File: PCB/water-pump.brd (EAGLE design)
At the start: 53 x 79.1 mm, 26 parts, among them U1 LDL1117S12R, U3 ATSAMD11C14A-SSUT

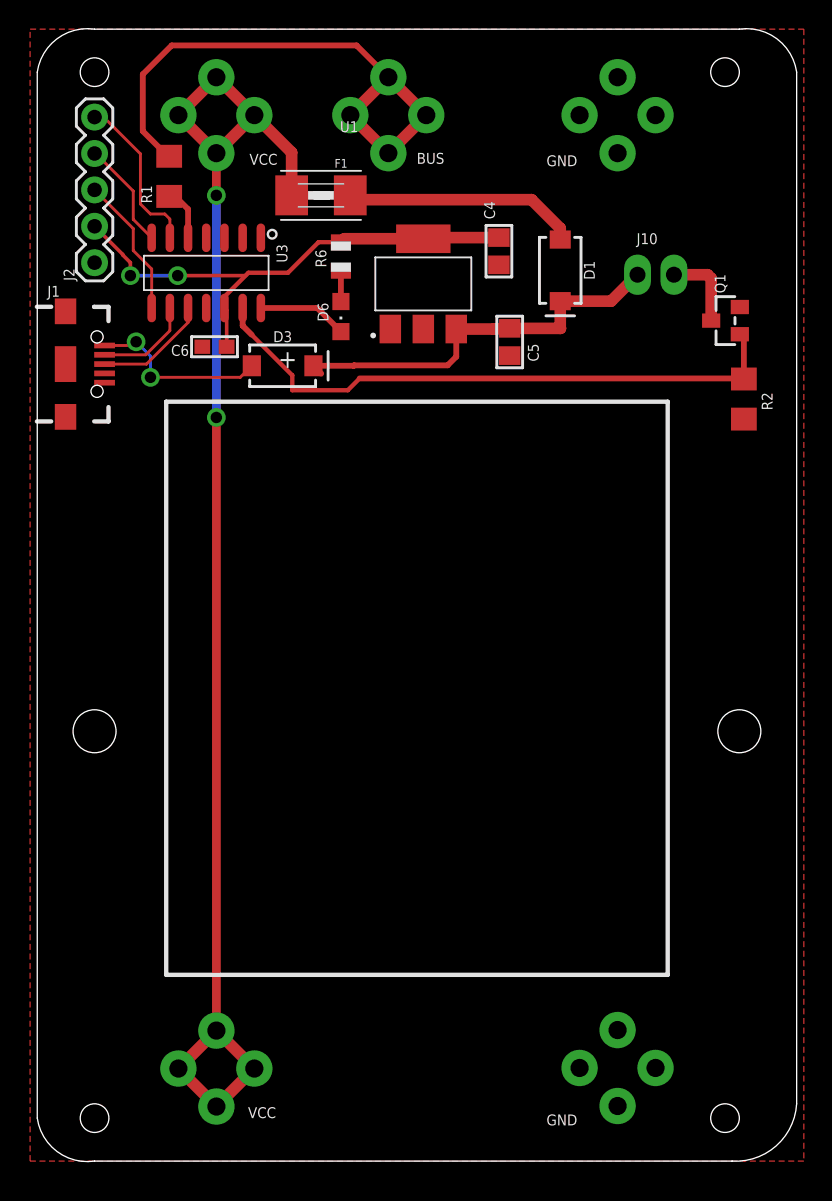
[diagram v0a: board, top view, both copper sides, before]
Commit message: added button to pcbs and did some fixing
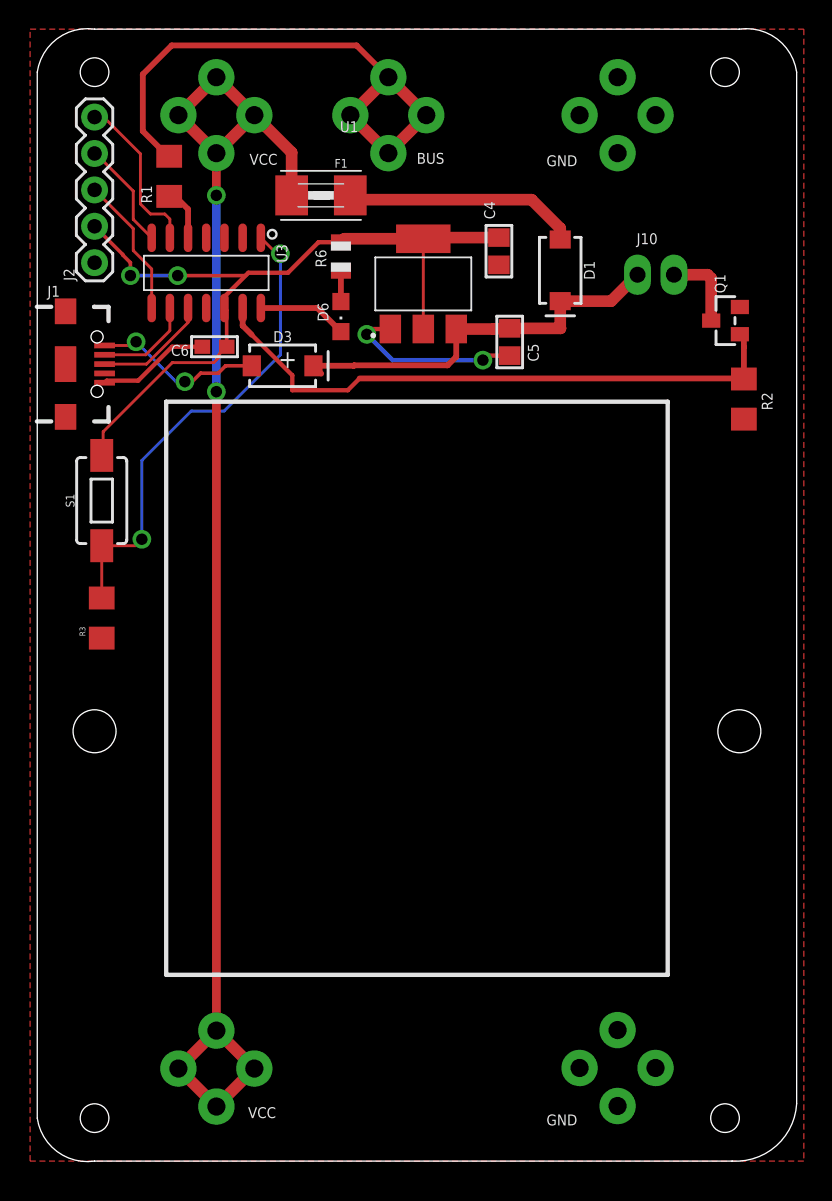
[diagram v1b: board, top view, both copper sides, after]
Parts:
- added R3: 2k, SparkFun-Resistors:1206
- added S1: MOMENTARY-SWITCH-SPST-SMD-6.0X3.5MM, SparkFun-Switches:TACTILE_SWITCH_SMD_6.0X3.5MM
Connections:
- new net N$4: R3.2, S1.1, U3.1
- net 3.3V: now also S1.2
- net GND: now also R3.1
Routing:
- net N$4: track 0.00 -> 33.7 mm, vias 0 -> 2
- net GND: track 0.00 -> 22.5 mm, vias 0 -> 2
- net 3.3V: track 37.2 -> 56.4 mm
- net N$1: track 12.6 -> 12.0 mm
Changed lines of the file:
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@@
 <?xml version="1.0" encoding="utf-8"?>
 <!DOCTYPE eagle SYSTEM "eagle.dtd">
-<eagle version="9.3.0">
+<eagle version="9.2.2">
 <drawing>
 <settings>
@@
 <attribute name="PACKAGE" value="SOIC-14 Microchip" x="11.795" y="61.989" size="1.778" layer="27" rot="R270" display="off"/>
 <attribute name="PRICE" value="1.18 USD" x="11.795" y="61.989" size="1.778" layer="27" rot="R270" display="off"/>
-<attribute name="VALUE" x="5.99306875" y="65.09003125" size="0.762" layer="27" font="vector" ratio="15" rot="R270"/>
 </element>
 <element name="D6" library="Adafruit" package="CHIPLED_0805" value="" x="21.193" y="58.941" smashed="yes" rot="R180">
@@
 <attribute name="NAME" x="21.6575" y="69.94" size="0.6096" layer="25" rot="R180"/>
 <attribute name="VALUE" x="21.6575" y="65.495" size="0.6096" layer="27" rot="R180"/>
+</element>
+<element name="R3" library="SparkFun-Resistors" package="1206" value="2k" x="4.5" y="37.9" smashed="yes" rot="R90">
+<attribute name="NAME" x="3.357" y="36.63" size="0.4064" layer="25" rot="R90"/>
+<attribute name="VALUE" x="6.024" y="36.503" size="0.4064" layer="27" rot="R90"/>
+</element>
+<element name="S1" library="SparkFun-Switches" package="TACTILE_SWITCH_SMD_6.0X3.5MM" value="MOMENTARY-SWITCH-SPST-SMD-6.0X3.5MM" x="4.5" y="46.1" smashed="yes" rot="R90">
+<attribute name="NAME" x="2.595" y="46.1" size="0.6096" layer="25" font="vector" ratio="20" rot="R90" align="bottom-center"/>
+<attribute name="PROD_ID" value="SWCH-00815" x="4.5" y="46.1" size="1.778" layer="27" rot="R90" display="off"/>
+<attribute name="SF_SKU" value="COM-08229" x="4.5" y="46.1" size="1.778" layer="27" rot="R90" display="off"/>
 </element>
 </elements>
@@
 <contactref element="Q1" pad="2"/>
 <contactref element="J1" pad="GND"/>
-<wire x1="40.502" y1="75.646" x2="43.15" y2="73" width="0" layer="19" extent="1-1"/>
-<wire x1="37.85" y1="73" x2="40.502" y2="75.646" width="0" layer="19" extent="1-1"/>
-<wire x1="40.502" y1="70.346" x2="43.15" y2="73" width="0" layer="19" extent="1-1"/>
-<wire x1="32.221" y1="62.553" x2="40.502" y2="70.346" width="0" layer="19" extent="1-1"/>
-<wire x1="32.973" y1="56.217" x2="32.221" y2="62.553" width="0" layer="19" extent="1-1"/>
-<wire x1="24.643" y1="58.071" x2="32.973" y2="56.217" width="0" layer="19" extent="1-1"/>
-<wire x1="11.521" y1="56.836" x2="24.643" y2="58.071" width="0" layer="19" extent="1-1"/>
-<wire x1="11.795" y1="59.539" x2="11.521" y2="56.836" width="0" layer="19" extent="1-1"/>
-<wire x1="4" y1="62.703" x2="11.795" y2="59.539" width="0" layer="19" extent="1-1"/>
-<wire x1="49.034" y1="59.609" x2="40.502" y2="70.346" width="0" layer="19" extent="1-1"/>
-<wire x1="49.317" y1="51.784" x2="49.034" y2="59.609" width="0" layer="19" extent="1-1"/>
-<wire x1="40.502" y1="9.146" x2="49.317" y2="51.784" width="0" layer="19" extent="1-1"/>
-<wire x1="43.15" y1="6.5" x2="40.502" y2="9.146" width="0" layer="19" extent="1-1"/>
-<wire x1="37.85" y1="6.5" x2="40.502" y2="9.146" width="0" layer="19" extent="1-1"/>
-<wire x1="40.502" y1="3.846" x2="43.15" y2="6.5" width="0" layer="19" extent="1-1"/>
-<wire x1="1.974" y1="59.309" x2="37.85" y2="6.5" width="0" layer="19" extent="1-1"/>
-<wire x1="1.974" y1="55.624" x2="1.974" y2="59.309" width="0" layer="19" extent="1-1"/>
-<wire x1="4.699" y1="54.324" x2="1.974" y2="55.624" width="0" layer="19" extent="1-1"/>
-<wire x1="1.974" y1="51.939" x2="4.699" y2="54.324" width="0" layer="19" extent="1-1"/>
+<contactref element="R3" pad="1"/>
+<wire x1="9.53020625" y1="56.836" x2="11.521" y2="56.836" width="0.2032" layer="1"/>
+<wire x1="4.699" y1="54.324" x2="4.8442" y2="54.4692" width="0.3048" layer="1"/>
+<wire x1="9.4107375" y1="56.836" x2="11.521" y2="56.836" width="0.3048" layer="1"/>
+<wire x1="4.8442" y1="54.4692" x2="7.0439375" y2="54.4692" width="0.3048" layer="1"/>
+<wire x1="7.0439375" y1="54.4692" x2="9.4107375" y2="56.836" width="0.3048" layer="1"/>
+<wire x1="32.973" y1="56.217" x2="31.417" y2="56.217" width="0.3048" layer="1"/>
+<wire x1="31.417" y1="56.217" x2="31.1" y2="55.9" width="0.3048" layer="1"/>
+<via x="31.1" y="55.9" extent="1-16" drill="0.8"/>
+<wire x1="31.1" y1="55.9" x2="24.8" y2="55.9" width="0.3048" layer="16"/>
+<wire x1="24.8" y1="55.9" x2="23" y2="57.7" width="0.3048" layer="16"/>
+<via x="23" y="57.7" extent="1-16" drill="0.8"/>
+<wire x1="23" y1="57.7" x2="23.371" y2="58.071" width="0.3048" layer="1"/>
+<wire x1="23.371" y1="58.071" x2="24.643" y2="58.071" width="0.3048" layer="1"/>
 </signal>
 <signal name="VCC-RAW" class="1">
@@
 <wire x1="15.15" y1="73" x2="17.754" y2="70.396" width="0.8128" layer="1"/>
 <wire x1="17.754" y1="70.396" x2="17.754" y2="67.4" width="0.8128" layer="1"/>
-<wire x1="12.5026" y1="51.8974" x2="12.5" y2="51.9" width="0.6096" layer="1"/>
-<via x="12.5" y="51.9" extent="1-16" drill="0.8"/>
-<wire x1="12.5" y1="51.9" x2="12.5" y2="67.4" width="0.6096" layer="16"/>
+<wire x1="12.5026" y1="53.6974" x2="12.5" y2="53.7" width="0.6096" layer="1"/>
+<via x="12.5" y="53.7" extent="1-16" drill="0.8"/>
+<wire x1="12.5" y1="53.7" x2="12.5" y2="67.4" width="0.6096" layer="16"/>
 <via x="12.5" y="67.4" extent="1-16" drill="0.8"/>
 <wire x1="12.5" y1="67.4" x2="12.5" y2="70.342" width="0.6096" layer="1"/>
 <wire x1="12.5" y1="70.342" x2="12.498" y2="70.344" width="0.6096" layer="1"/>
-<wire x1="12.5026" y1="9.1074" x2="12.5026" y2="51.8974" width="0.6096" layer="1"/>
+<wire x1="12.5026" y1="9.1074" x2="12.5026" y2="53.6974" width="0.6096" layer="1"/>
 </signal>
 <signal name="BUS">
@@
 <signal name="PUMP_CTRL">
 <contactref element="R2" pad="1"/>
-<wire x1="49.317" y1="57.426" x2="49.317" y2="54.623" width="0.4064" layer="1"/>
 <contactref element="U3" pad="13"/>
+<wire x1="49.317" y1="56.8" x2="49.317" y2="54.623" width="0.4064" layer="1"/>
 <wire x1="49.317" y1="54.623" x2="49.317" y2="54.584" width="0.4064" layer="1"/>
 <wire x1="14.335" y1="59.539" x2="14.335" y2="58.306" width="0.4064" layer="1"/>
@@
 <wire x1="17.8" y1="53.8" x2="17.8" y2="54.841" width="0.3048" layer="1"/>
 <wire x1="17.8" y1="54.841" x2="14.97" y2="57.671" width="0.3048" layer="1"/>
-<wire x1="49.317" y1="57.426" x2="49.034" y2="57.709" width="0" layer="19" extent="1-1"/>
+<wire x1="49.317" y1="56.8" x2="49.317" y2="57.426" width="0.4064" layer="1"/>
+<wire x1="49.317" y1="57.426" x2="49.034" y2="57.709" width="0.4064" layer="1"/>
 </signal>
 <signal name="PUMP">
@@
 <wire x1="6.642" y1="56.924" x2="6.9" y2="57.182" width="0.2032" layer="1"/>
 <via x="6.9" y="57.182" extent="1-16" drill="0.8"/>
-<wire x1="6.9" y1="57.182" x2="7.9" y2="56.182" width="0.2032" layer="16"/>
-<wire x1="7.9" y1="56.182" x2="7.9" y2="54.7" width="0.2032" layer="16"/>
-<via x="7.9" y="54.7" extent="1-16" drill="0.8"/>
-<wire x1="7.9" y1="54.7" x2="14.168" y2="54.7" width="0.2032" layer="1"/>
-<wire x1="14.168" y1="54.7" x2="14.975" y2="55.507" width="0.2032" layer="1"/>
+<wire x1="6.9" y1="57.182" x2="9.682" y2="54.4" width="0.2032" layer="16"/>
+<wire x1="9.682" y1="54.4" x2="10.3" y2="54.4" width="0.2032" layer="16"/>
+<via x="10.3" y="54.4" extent="1-16" drill="0.8"/>
+<wire x1="10.6" y1="54.4" x2="10.3" y2="54.4" width="0.2032" layer="1"/>
+<wire x1="14.975" y1="55.507" x2="13.14581875" y2="55.507" width="0.254" layer="1"/>
+<wire x1="13.14581875" y1="55.507" x2="12.62861875" y2="54.9898" width="0.254" layer="1"/>
+<wire x1="12.62861875" y1="54.9898" x2="11.4" y2="54.9898" width="0.254" layer="1"/>
+<wire x1="11.4" y1="54.9898" x2="10.8102" y2="54.4" width="0.254" layer="1"/>
+<wire x1="10.8102" y1="54.4" x2="10.6" y2="54.4" width="0.254" layer="1"/>
 </signal>
 <signal name="RESET">
@@
 <wire x1="9.8" y1="61.8" x2="14.5377875" y2="61.8" width="0.254" layer="1"/>
 <wire x1="14.5377875" y1="61.8" x2="14.7377875" y2="62" width="0.254" layer="1"/>
-<wire x1="26.943" y1="64.371" x2="26.943" y2="58.071" width="0" layer="19" extent="1-1"/>
+<contactref element="S1" pad="2"/>
+<wire x1="4.5" y1="49.25" x2="4.6" y2="49.35" width="0.2032" layer="1"/>
+<wire x1="4.6" y1="49.35" x2="4.6" y2="50.9" width="0.2032" layer="1"/>
+<wire x1="12.32350625" y1="55.7264" x2="12.6806" y2="56.08349375" width="0.2032" layer="1"/>
+<wire x1="4.6" y1="50.9" x2="9.4264" y2="55.7264" width="0.2032" layer="1"/>
+<wire x1="12.6806" y1="56.08349375" x2="12.6806" y2="56.2956" width="0.2032" layer="1"/>
+<wire x1="12.6806" y1="56.2956" x2="13.221" y2="56.836" width="0.2032" layer="1"/>
+<wire x1="9.4264" y1="55.7264" x2="12.32350625" y2="55.7264" width="0.2032" layer="1"/>
+<wire x1="26.943" y1="58.071" x2="26.943" y2="64.371" width="0.2032" layer="1"/>
+</signal>
+<signal name="N$4">
+<contactref element="R3" pad="2"/>
+<contactref element="S1" pad="1"/>
+<contactref element="U3" pad="1"/>
+<wire x1="15.605" y1="64.439" x2="16.714578125" y2="63.329421875" width="0.2032" layer="1"/>
+<wire x1="16.714578125" y1="63.329421875" x2="16.970578125" y2="63.329421875" width="0.2032" layer="1"/>
+<via x="16.970578125" y="63.329421875" extent="1-16" drill="0.8"/>
+<wire x1="16.970578125" y1="56.270578125" x2="16.970578125" y2="63.329421875" width="0.2032" layer="16"/>
+<wire x1="13.05" y1="52.35" x2="16.970578125" y2="56.270578125" width="0.2032" layer="16"/>
+<via x="7.3" y="43.4" extent="1-16" drill="0.8"/>
+<wire x1="7.3" y1="43.4" x2="6.85" y2="42.95" width="0.2032" layer="1"/>
+<wire x1="6.85" y1="42.95" x2="4.5" y2="42.95" width="0.2032" layer="1"/>
+<wire x1="4.5" y1="42.95" x2="4.5" y2="39.3" width="0.2032" layer="1"/>
+<wire x1="10.75" y1="52.35" x2="13.05" y2="52.35" width="0.2032" layer="16"/>
+<wire x1="7.3" y1="43.4" x2="7.3" y2="48.9" width="0.2032" layer="16"/>
+<wire x1="7.3" y1="48.9" x2="10.75" y2="52.35" width="0.2032" layer="16"/>
 </signal>
 </signals>

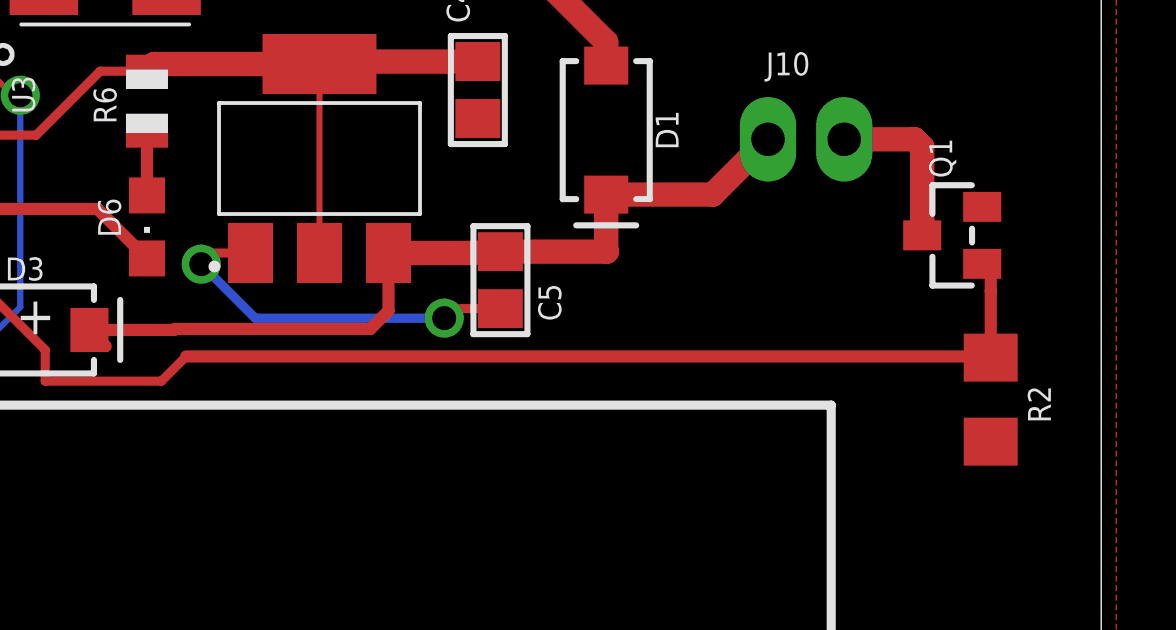
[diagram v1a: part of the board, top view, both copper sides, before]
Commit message: added missing resistor before mosfet
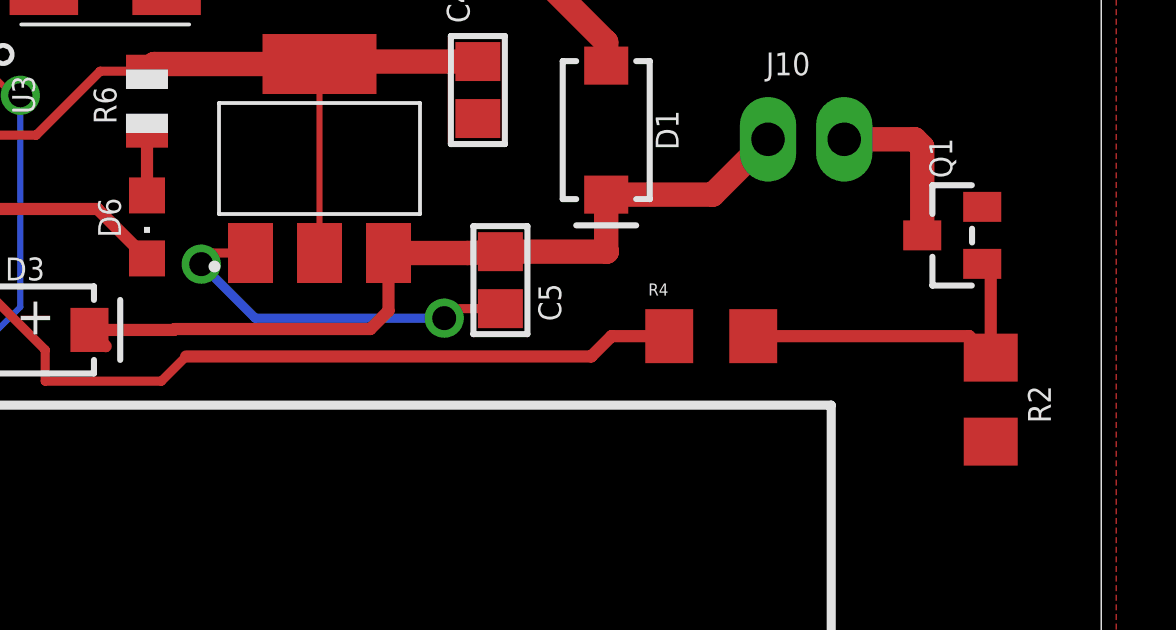
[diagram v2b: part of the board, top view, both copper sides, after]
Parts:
- added R4: 499R, SparkFun-Resistors:1206
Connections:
- new net N$5: Q1.1, R2.1, R4.1
- net PUMP_CTRL: now also R4.2; no longer Q1.1, R2.1
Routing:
- net PUMP_CTRL: track 42.3 -> 28.6 mm
- net N$5: track 0.00 -> 11.5 mm
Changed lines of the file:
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@@
 <?xml version="1.0" encoding="utf-8"?>
 <!DOCTYPE eagle SYSTEM "eagle.dtd">
-<eagle version="9.2.2">
+<eagle version="9.3.0">
 <drawing>
 <settings>
@@
 <attribute name="SF_SKU" value="COM-08229" x="4.5" y="46.1" size="1.778" layer="27" rot="R90" display="off"/>
 </element>
+<element name="R4" library="SparkFun-Resistors" package="1206" value="499R" x="40" y="55.3" smashed="yes" rot="R180">
+<attribute name="NAME" x="38.57" y="57.057" size="0.4064" layer="25" rot="R180"/>
+<attribute name="VALUE" x="40.997" y="57.024" size="0.4064" layer="27" rot="R180"/>
+</element>
 </elements>
 <signals>
@@
 </signal>
 <signal name="PUMP_CTRL">
-<contactref element="R2" pad="1"/>
 <contactref element="U3" pad="13"/>
-<wire x1="49.317" y1="56.8" x2="49.317" y2="54.623" width="0.4064" layer="1"/>
-<wire x1="49.317" y1="54.623" x2="49.317" y2="54.584" width="0.4064" layer="1"/>
 <wire x1="14.335" y1="59.539" x2="14.335" y2="58.306" width="0.4064" layer="1"/>
-<wire x1="49.317" y1="54.623" x2="22.496" y2="54.623" width="0.4064" layer="1"/>
+<wire x1="36" y1="54.623" x2="22.496" y2="54.623" width="0.4064" layer="1"/>
 <wire x1="14.97" y1="57.671" x2="14.335" y2="58.306" width="0.4064" layer="1"/>
-<contactref element="Q1" pad="1"/>
 <wire x1="22.496" y1="54.623" x2="21.673" y2="53.8" width="0.3048" layer="1"/>
 <wire x1="21.673" y1="53.8" x2="17.8" y2="53.8" width="0.3048" layer="1"/>
 <wire x1="17.8" y1="53.8" x2="17.8" y2="54.841" width="0.3048" layer="1"/>
 <wire x1="17.8" y1="54.841" x2="14.97" y2="57.671" width="0.3048" layer="1"/>
-<wire x1="49.317" y1="56.8" x2="49.317" y2="57.426" width="0.4064" layer="1"/>
-<wire x1="49.317" y1="57.426" x2="49.034" y2="57.709" width="0.4064" layer="1"/>
+<contactref element="R4" pad="2"/>
+<wire x1="36" y1="54.623" x2="36.677" y2="55.3" width="0.4064" layer="1"/>
+<wire x1="36.677" y1="55.3" x2="38.6" y2="55.3" width="0.4064" layer="1"/>
 </signal>
 <signal name="PUMP">
@@
 <wire x1="7.3" y1="48.9" x2="10.75" y2="52.35" width="0.2032" layer="16"/>
 </signal>
+<signal name="N$5">
+<contactref element="R2" pad="1"/>
+<contactref element="Q1" pad="1"/>
+<contactref element="R4" pad="1"/>
+<wire x1="49.317" y1="57.426" x2="49.317" y2="54.584" width="0.4064" layer="1"/>
+<wire x1="49.317" y1="57.426" x2="49.034" y2="57.709" width="0.4064" layer="1"/>
+<wire x1="41.4" y1="55.3" x2="48.601" y2="55.3" width="0.4064" layer="1"/>
+<wire x1="48.601" y1="55.3" x2="49.317" y2="54.584" width="0.4064" layer="1"/>
+</signal>
 </signals>
